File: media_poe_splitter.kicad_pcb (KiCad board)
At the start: 2 copper layers, 70.7 x 75 mm, 30 parts, among them J1 Screw_Terminal_01x02, X1 7499811120

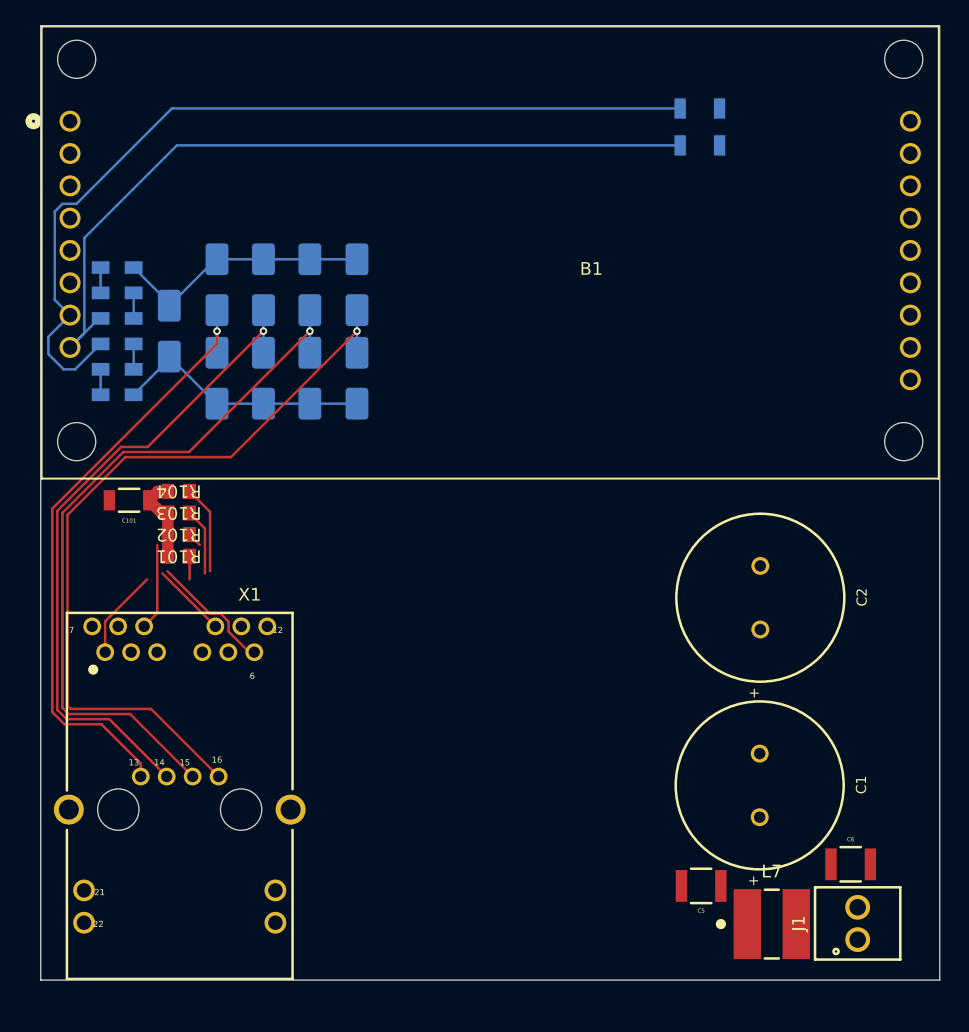
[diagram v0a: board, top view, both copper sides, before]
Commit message: poe: add missing tracks
Signed-off-by: Marc 'risson' Schmitt <marc.schmitt@risson.space>
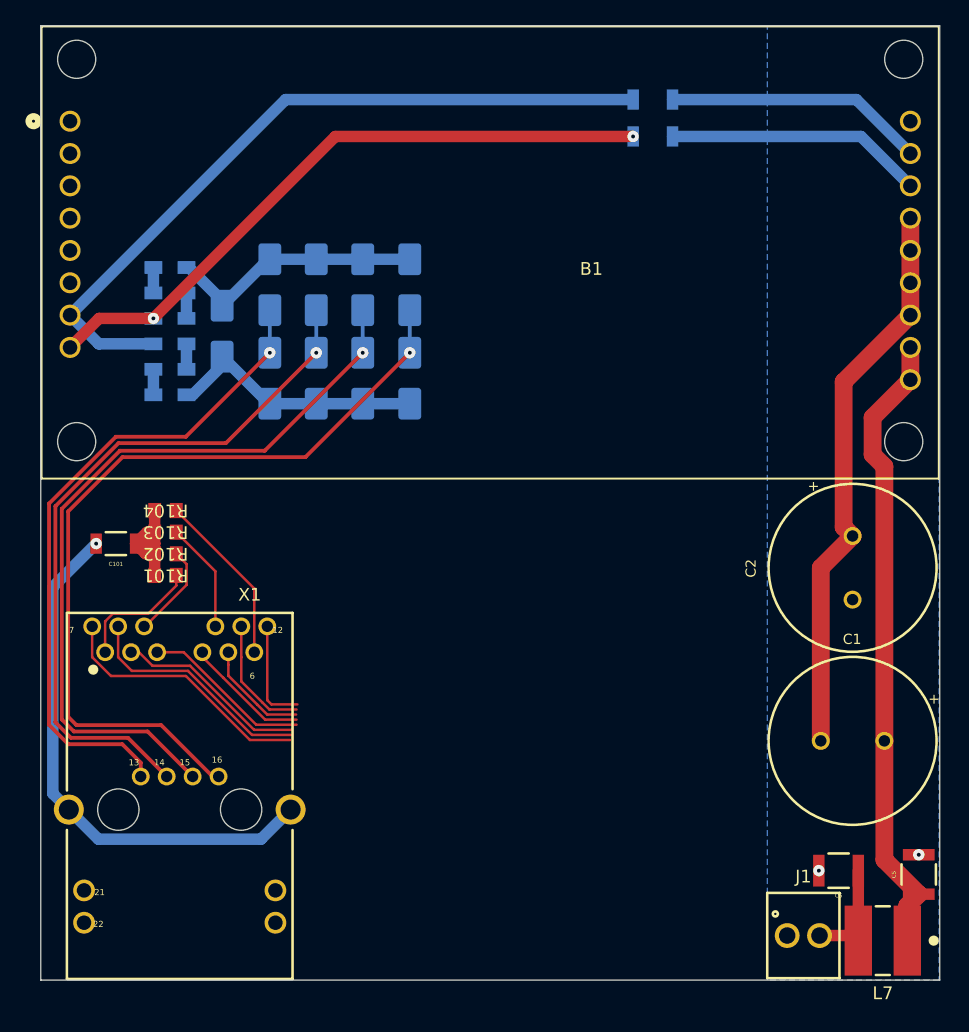
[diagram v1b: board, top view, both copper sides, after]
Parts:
- moved C5 17.1 mm to (89.0, 86.7), turned to 90 degrees
- moved L7 8.82 mm to (86.2, 91.9), turned to 180 degrees
- moved C1 8.10 mm to (83.8, 76.2), turned to 0 degrees
- moved C2 7.62 mm to (83.8, 62.6), turned to 90 degrees
- moved J1 4.37 mm to (79.9, 91.5), turned to 0 degrees
- moved D1 4.15 mm to (34.2, 44.0)
- moved D2 4.15 mm to (49.0, 40.4)
- moved D3 4.15 mm to (49.0, 47.7)
- moved D4 4.15 mm to (45.3, 40.4)
- moved D5 4.15 mm to (45.3, 47.7)
- moved D6 4.15 mm to (41.6, 40.4)
- moved D7 4.15 mm to (41.6, 47.7)
- moved D8 4.15 mm to (38.0, 40.4)
- moved D9 4.15 mm to (38.0, 47.7)
- moved L1 4.15 mm to (30.1, 39.0)
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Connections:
- J1 pad 1: +24V -> GNDA
- J1 pad 2: GNDA -> +24V
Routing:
- net Net-(B1-VOUT2-Pad10): track 0.92 -> 49.7 mm
- net Net-(B1-0V2-Pad11): track 0.00 -> 44.6 mm
- net GNDPWR: track 0.00 -> 42.2 mm, vias 0 -> 1
- net GNDA: track 0.00 -> 40.7 mm, vias 0 -> 2
- net unconnected-(X1-TRD1+-Pad7): track 0.00 -> 20.7 mm
- net unconnected-(X1-TRD1--Pad8): track 0.00 -> 18.7 mm
- net unconnected-(X1-TRD2+-Pad2): track 0.00 -> 15.2 mm
- net unconnected-(X1-TRD2--Pad3): track 0.00 -> 13.3 mm
- net Net-(B1-VIN-): track 70.3 -> 58.8 mm
- net Net-(B1-VIN+): track 62.3 -> 51.2 mm, vias 0 -> 2
- net unconnected-(X1-TRD3+-Pad4): track 0.00 -> 10.2 mm
- net unconnected-(X1-TRD4+-Pad11): track 0.00 -> 9.58 mm
- net unconnected-(X1-TRD3--Pad5): track 0.00 -> 8.44 mm
- net unconnected-(X1-TRD4--Pad12): track 0.00 -> 8.31 mm
- net +24V: track 1.97 -> 8.72 mm
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- added copper zone on B.Cu, net GNDA

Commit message: add USB controller, finish board
Signed-off-by: Marc 'risson' Schmitt <marc.schmitt@risson.space>
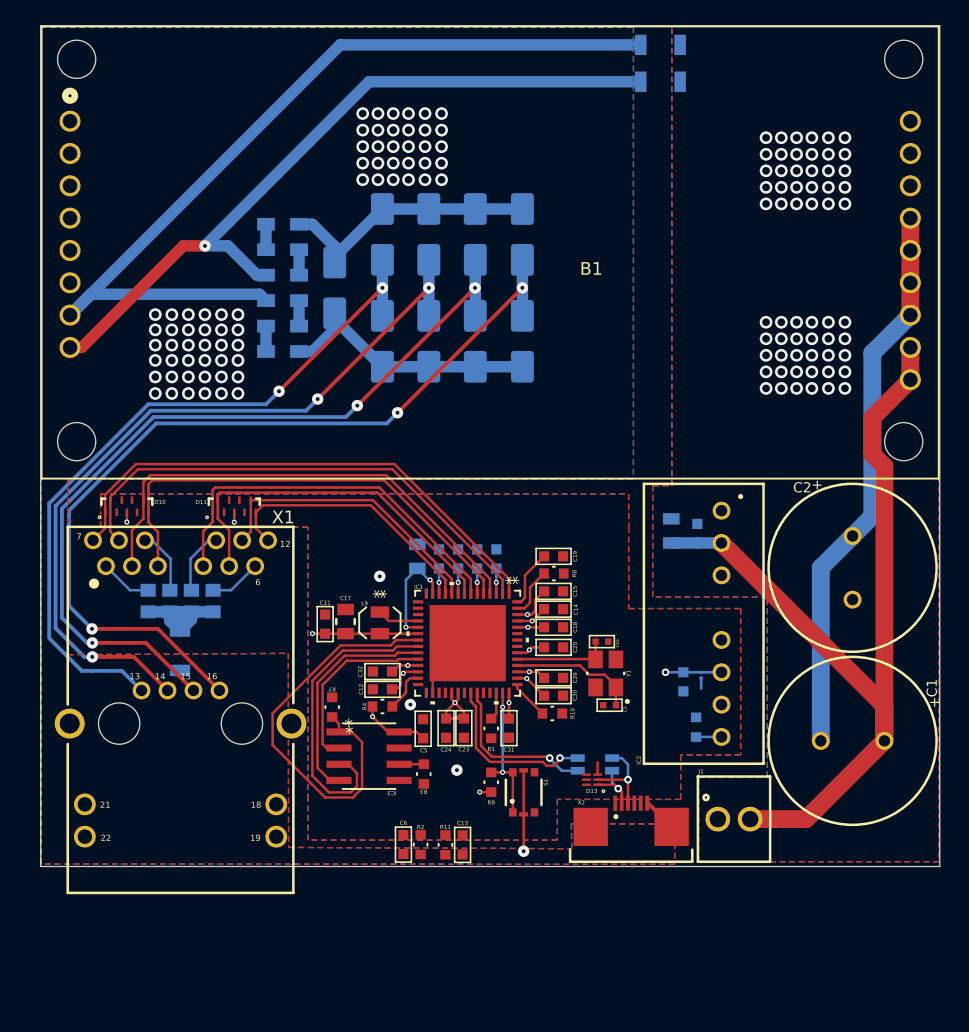
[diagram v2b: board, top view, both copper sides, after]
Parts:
- added C10: 100nF 25V, 885012206071:885012206071, B.Cu at (70.5, 71.6)
- added C11: 100nF 25V, 885012206071:885012206071, F.Cu at (42.3, 67.0)
- added C12: 100nF 25V, 885012206071:885012206071, F.Cu at (46.8, 72.1)
- added C13: 100nF 25V, 885012206071:885012206071, F.Cu at (53.1, 84.4)
- added C14: 1uF 16V, 885012206052:885012206052, F.Cu at (60.3, 65.8)
- added C15: 1uF 16V, 885012206052:885012206052, F.Cu at (60.3, 64.4)
- added C16: 15pF 50V, 885012005056:885012005056, F.Cu at (64.1, 68.4)
- added C17: 10uF 6.3V, 885012207003:885012207003, F.Cu at (43.9, 66.8)
- added C18: 100nF 25V, 885012206071:885012206071, F.Cu at (60.3, 67.3)
- added C19: 1uF 16V, 885012206052:885012206052, F.Cu at (60.3, 61.7)
- added C20: 100nF 25V, 885012206071:885012206071, F.Cu at (60.3, 68.8)
- added C23: 100nF 25V, 885012206071:885012206071, F.Cu at (53.2, 75.2)
- added C24: 100nF 25V, 885012206071:885012206071, F.Cu at (51.8, 75.2)
- added C25: 100nF 25V, 885012206071:885012206071, B.Cu at (51.3, 61.9)
- added C26: 100nF 25V, 885012206071:885012206071, B.Cu at (54.3, 61.9)
- added C27: 100nF 25V, 885012206071:885012206071, B.Cu at (55.8, 61.9)
- added C28: 100nF 25V, 885012206071:885012206071, B.Cu at (52.8, 61.9)
- added C29: 100nF 25V, 885012206071:885012206071, F.Cu at (60.3, 71.2)
- added C3: 15pF 50V, 885012005056:885012005056, F.Cu at (64.7, 73.4)
- added C30: 100nF 25V, 885012206071:885012206071, F.Cu at (60.3, 72.6)
- added C31: 100nF 25V, 885012206071:885012206071, F.Cu at (56.8, 75.2)
- added C32: 100nF 25V, 885012206071:885012206071, F.Cu at (46.8, 70.7)
- added C33: 10uF 6.3V, 885012207003:885012207003, B.Cu at (49.6, 61.7)
- added C4: 2.2uF 25V, 885012207079:885012207079, B.Cu at (69.5, 59.7)
- added C7: 100nF 25V, 885012206071:885012206071, B.Cu at (71.6, 59.9)
- added C8: 10nF 6.3V, 885012104004:885012104004, B.Cu at (71.9, 71.0)
- added D10: 5Vdc, 824014885:824014885, F.Cu at (26.8, 57.8)
- added D11: 5Vdc, 824014885:824014885, F.Cu at (35.2, 57.8)
- added D13: 824012823, 824012823:824012823, F.Cu at (63.3, 79.2)
- added IC1: LAN7850-I_8JX, LAN7850-I_8JX:LAN7850-I_8JX, F.Cu at (53.5, 68.5)
- added IC2: 17791063215, 17791063215:17791063215, F.Cu at (72.1, 67.0)
- added IC3: 93AA66C-I/SN, 93AA66C-I_SN:93AA66C-I_SN, F.Cu at (45.8, 77.4)
- added L9: VLF302515MT-3R3M, VLF302515MT-3R3M:VLF302515MT-3R3M, F.Cu at (46.6, 66.9)
- added R1: 10K, RC0603FR-0710KL:RC0603FR-0710KL, F.Cu at (55.4, 75.2)
- added R10: 12K, RC0603FR-0712KL:RC0603FR-0712KL, F.Cu at (60.2, 74.0)
- added R11: 330R, RC0603FR-07340RL:RC0603FR-07340RL, F.Cu at (51.8, 84.4)
- added R2: 330R, RC0603FR-07340RL:RC0603FR-07340RL, F.Cu at (49.9, 84.3)
- added R3: 10K, RC0603FR-0710KL:RC0603FR-0710KL, F.Cu at (50.1, 78.8)
- added R4: 10K, RC0603FR-0710KL:RC0603FR-0710KL, F.Cu at (46.8, 73.5)
- added R6: 47.8K, RC0603FR-0748K7L:RC0603FR-0748K7L, B.Cu at (71.5, 75.1)
- added R7: 10K, RC0603FR-0710KL:RC0603FR-0710KL, F.Cu at (42.9, 73.5)
- added R8: 2K, RC0603FR-072KL:RC0603FR-072KL, F.Cu at (60.3, 63.0)
- added R9: 100K, RC0603FR-07100KL:RC0603FR-07100KL, F.Cu at (55.4, 79.5)
- added S1: 435151014824, 435151014824:435151014824, F.Cu at (57.9, 80.3)
- added X2: 68710614522, 68710614522:68710614522, F.Cu at (66.4, 83.5)
- added Y1: 830055299, 830055299:830055299, F.Cu at (64.4, 70.9)
- C101, R101, R102, R103, R104: moved to B.Cu
- C5, C6: value 10uF -> 100nF 25V; footprint 885012209073:885012209073 -> 885012206071:885012206071
- L7: value 2.2uH -> 744232090; footprint 744774022:744774022 -> 744232090:744232090; moved to B.Cu
- moved C5 40.6 mm to (50.0, 75.2), turned to -90 degrees
- moved C6 34.3 mm to (48.5, 84.3), turned to -90 degrees
- moved L7 26.5 mm to (63.5, 78.0)
- moved J1 10.7 mm to (74.5, 82.3)
- moved C101 9.81 mm to (30.9, 69.1), turned to -90 degrees
- moved D2 9.69 mm to (57.9, 36.4)
- moved D4 9.69 mm to (54.1, 36.4)
- moved D6 9.69 mm to (50.5, 36.4)
- moved D8 9.69 mm to (46.9, 36.4)
- moved D1 9.48 mm to (43.1, 40.6)
- moved L1 9.48 mm to (39.0, 35.6)
- moved L2 9.48 mm to (39.0, 37.6)
- moved L3 9.48 mm to (39.0, 39.6)
- moved L4 9.48 mm to (39.0, 45.6)
- moved L5 9.48 mm to (39.0, 43.6)
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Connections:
- B1 pad 10: Net-(B1-VOUT2-Pad10) -> +24V
- B1 pad 9: Net-(B1-VOUT2-Pad10) -> +24V
- C1 pad 1: Net-(B1-VOUT2-Pad10) -> +24V
- C5 pad 1: Net-(B1-VOUT2-Pad10) -> GND
- C5 pad 2: GNDA -> +3V3
- C6 pad 1: +24V -> GND
- C6 pad 2: GNDA -> GNDPWR
- L7 pad 1: Net-(B1-VOUT2-Pad10) -> Net-(D13-Pad2)
- L7 pad 2: +24V -> /USBD_P
- X1 pad 11: unconnected-(X1-TRD4+-Pad11) -> /TR3_P
- X1 pad 12: unconnected-(X1-TRD4--Pad12) -> /TR3_N
- X1 pad 2: unconnected-(X1-TRD2+-Pad2) -> /TR1_P
- X1 pad 3: unconnected-(X1-TRD2--Pad3) -> /TR1_N
- X1 pad 4: unconnected-(X1-TRD3+-Pad4) -> /TR2_P
- X1 pad 5: unconnected-(X1-TRD3--Pad5) -> /TR2_N
- X1 pad 7: unconnected-(X1-TRD1+-Pad7) -> /TR0_P
- X1 pad 8: unconnected-(X1-TRD1--Pad8) -> /TR0_N
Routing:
- net +3V3: track 0.00 -> 84.5 mm, vias 0 -> 10
- net +24V: track 8.72 -> 70.4 mm
- net +1V2: track 0.00 -> 55.1 mm, vias 0 -> 5
- net Net-(B1-VOUT2-Pad10): track 49.7 -> 0.00 mm
- net /TR0_P: track 0.00 -> 41.6 mm
- net GNDA: track 40.7 -> 0.00 mm, vias 2 -> 60
- net /TR0_N: track 0.00 -> 40.1 mm
- net /TR1_P: track 0.00 -> 39.6 mm
- net /TR1_N: track 0.00 -> 37.5 mm
- net GNDPWR: track 42.2 -> 9.06 mm, vias 1 -> 67
- net Net-(IC1-EECS/GPIO1): track 0.00 -> 32.5 mm
- net /TR2_P: track 0.00 -> 31.6 mm
- net /TR2_N: track 0.00 -> 29.4 mm
- net Net-(IC1-EEDI/GPIO2): track 0.00 -> 23.9 mm
- net /TR3_P: track 0.00 -> 22.9 mm
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- added copper zone on B.Cu, net GND
- added copper zone on F.Cu, net GND
- added copper zone on In1.Cu, net GND
- added copper zone on In2.Cu, net GND
- added copper zone on F.Cu, net GNDA
- added copper zone on In1.Cu, net GNDA
- added copper zone on In2.Cu, net GNDA
- added copper zone on B.Cu, net GNDPWR
- added copper zone on F.Cu, net GNDPWR
- added copper zone on In1.Cu, net GNDPWR
- added copper zone on In2.Cu, net GNDPWR
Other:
- board size 70.7 x 75 mm -> 70.7 x 66.1 mm
- copper layers 2 -> 4

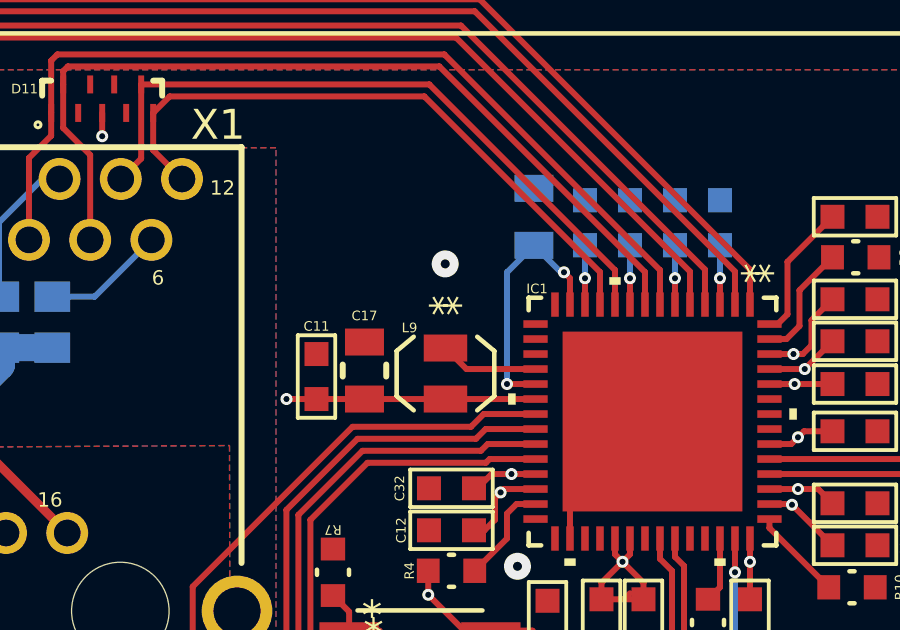
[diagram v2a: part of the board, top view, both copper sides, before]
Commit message: replace NLA part
Signed-off-by: Marc 'risson' Schmitt <marc.schmitt@risson.space>
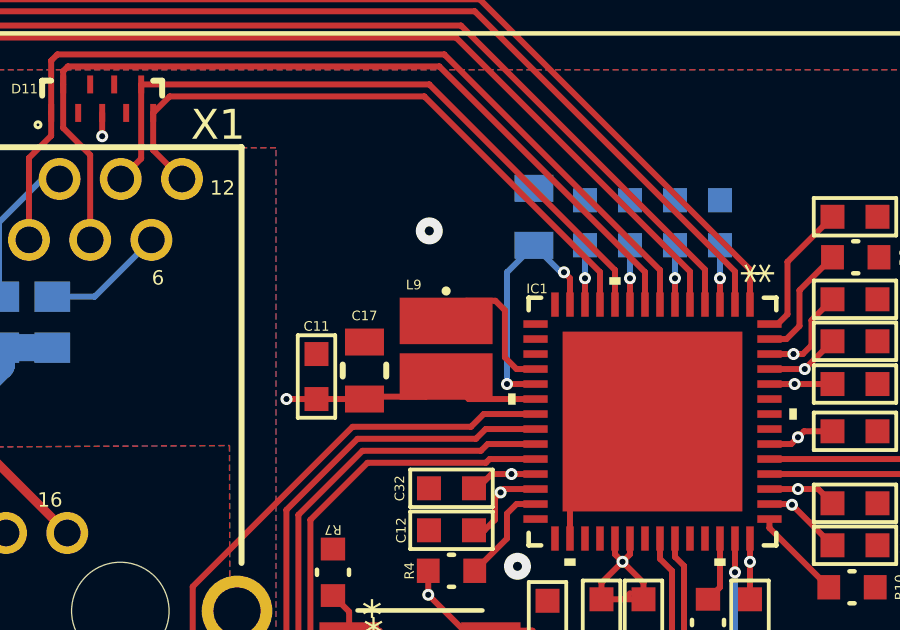
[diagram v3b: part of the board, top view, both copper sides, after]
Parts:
- L9: value VLF302515MT-3R3M -> VLS3012HBX-3R3M; footprint VLF302515MT-3R3M:VLF302515MT-3R3M -> VLS3012HBX-3R3M:VLS3012HBX-3R3M
- moved L9 0.83 mm to (46.7, 66.1)
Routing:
- net Net-(IC1-VDD12_SW_OUT): track 3.29 -> 5.12 mm
- net +1V2: track 55.1 -> 55.7 mm

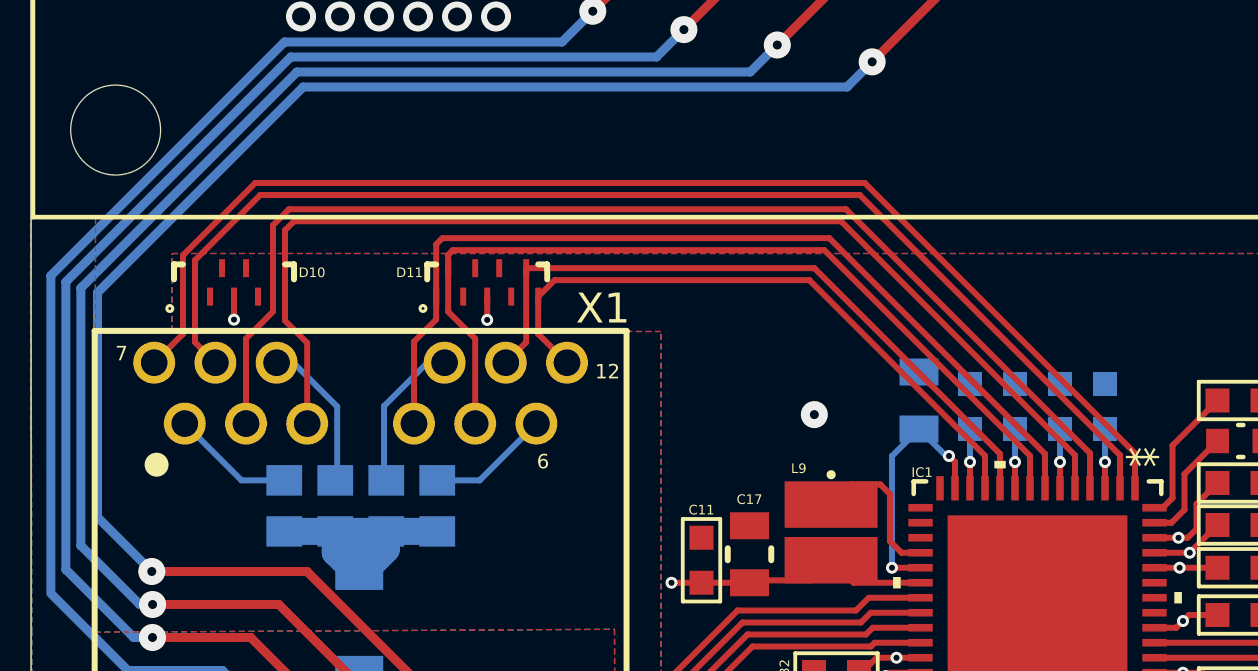
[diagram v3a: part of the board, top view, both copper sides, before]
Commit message: board: try to make sure that ethernet tracks have the same length
Signed-off-by: Marc 'risson' Schmitt <marc.schmitt@risson.space>
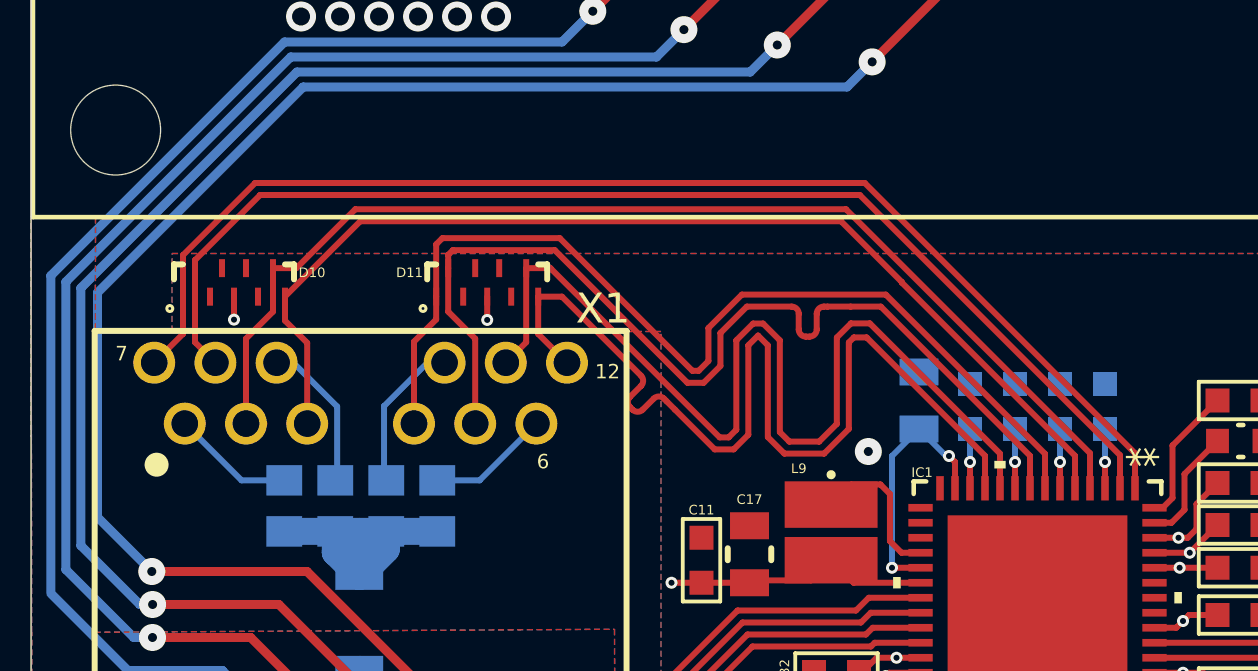
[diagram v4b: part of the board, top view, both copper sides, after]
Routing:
- net /TR3_N: track 21.2 -> 33.9 mm
- net /TR3_P: track 22.9 -> 34.6 mm
- net /TR2_N: track 29.4 -> 33.7 mm
- net /TR2_P: track 31.6 -> 34.3 mm
- net /TR1_N: track 37.5 -> 36.2 mm
- net /TR1_P: track 39.6 -> 38.8 mm
